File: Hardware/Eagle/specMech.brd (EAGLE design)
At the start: 142.2 x 121.9 mm, 80 parts, among them J1 PINHD-1X8-MOLEX-SHROUD, J2 JST-2-PIN-2B-PH-K-S(LF)(SN), J3 PINHD-1X8-MOLEX-SHROUD, J4 PINHD-1X8-MOLEX-SHROUD, J6 Molex 0022232081, J8 Molex 0022232081, U1 MCP23008-E/SO, U10 ADS1115, U11 MCP23008-E/SO, U12 74HC2G17TSSOP-6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

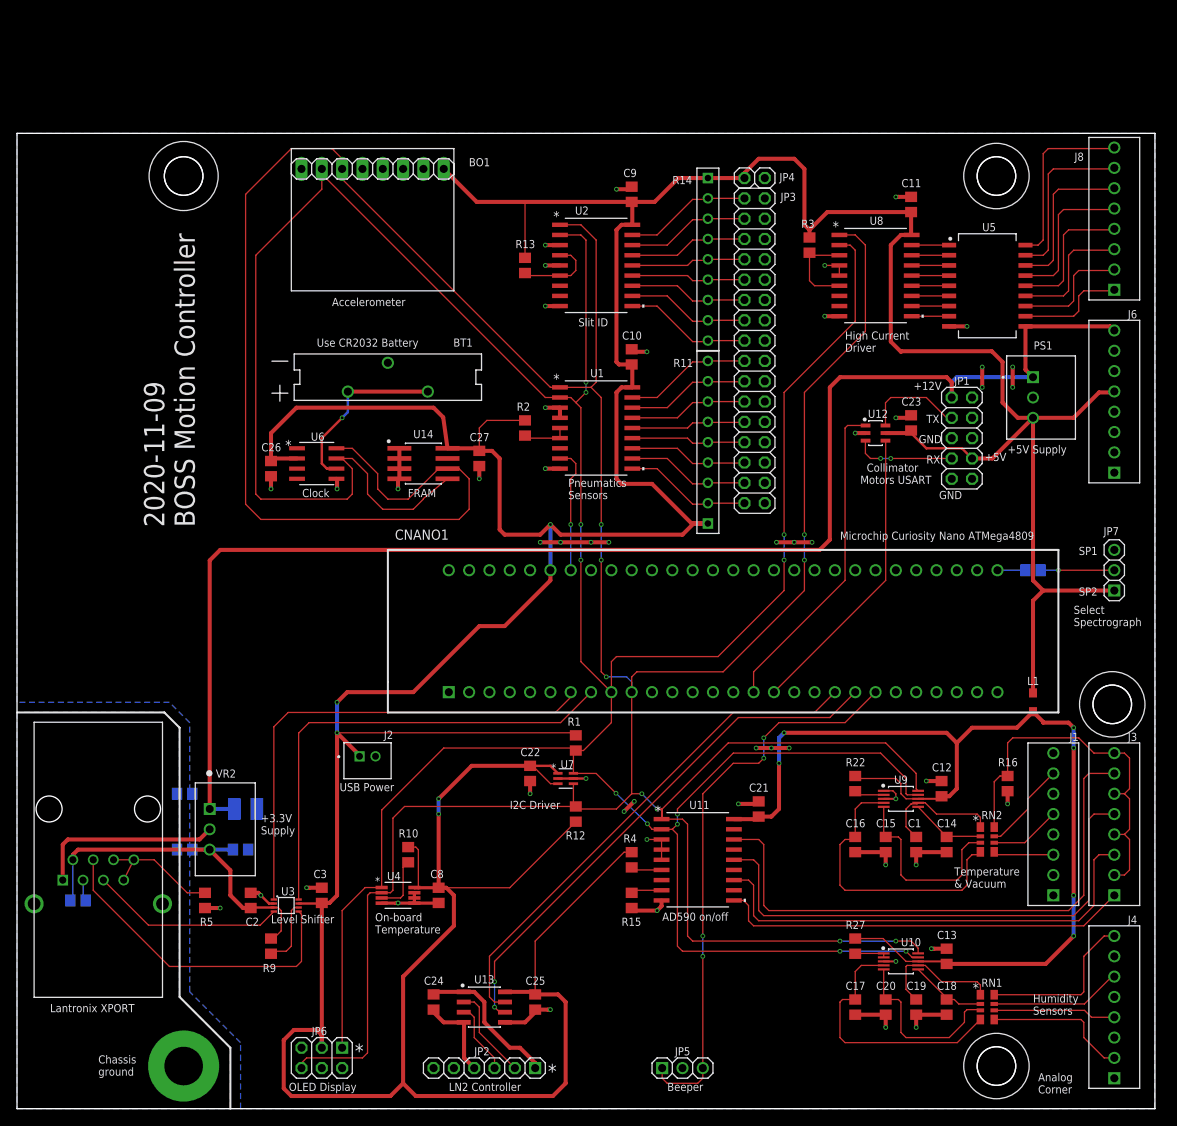
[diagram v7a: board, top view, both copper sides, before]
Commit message: Added test points, changed conflicting i2c address
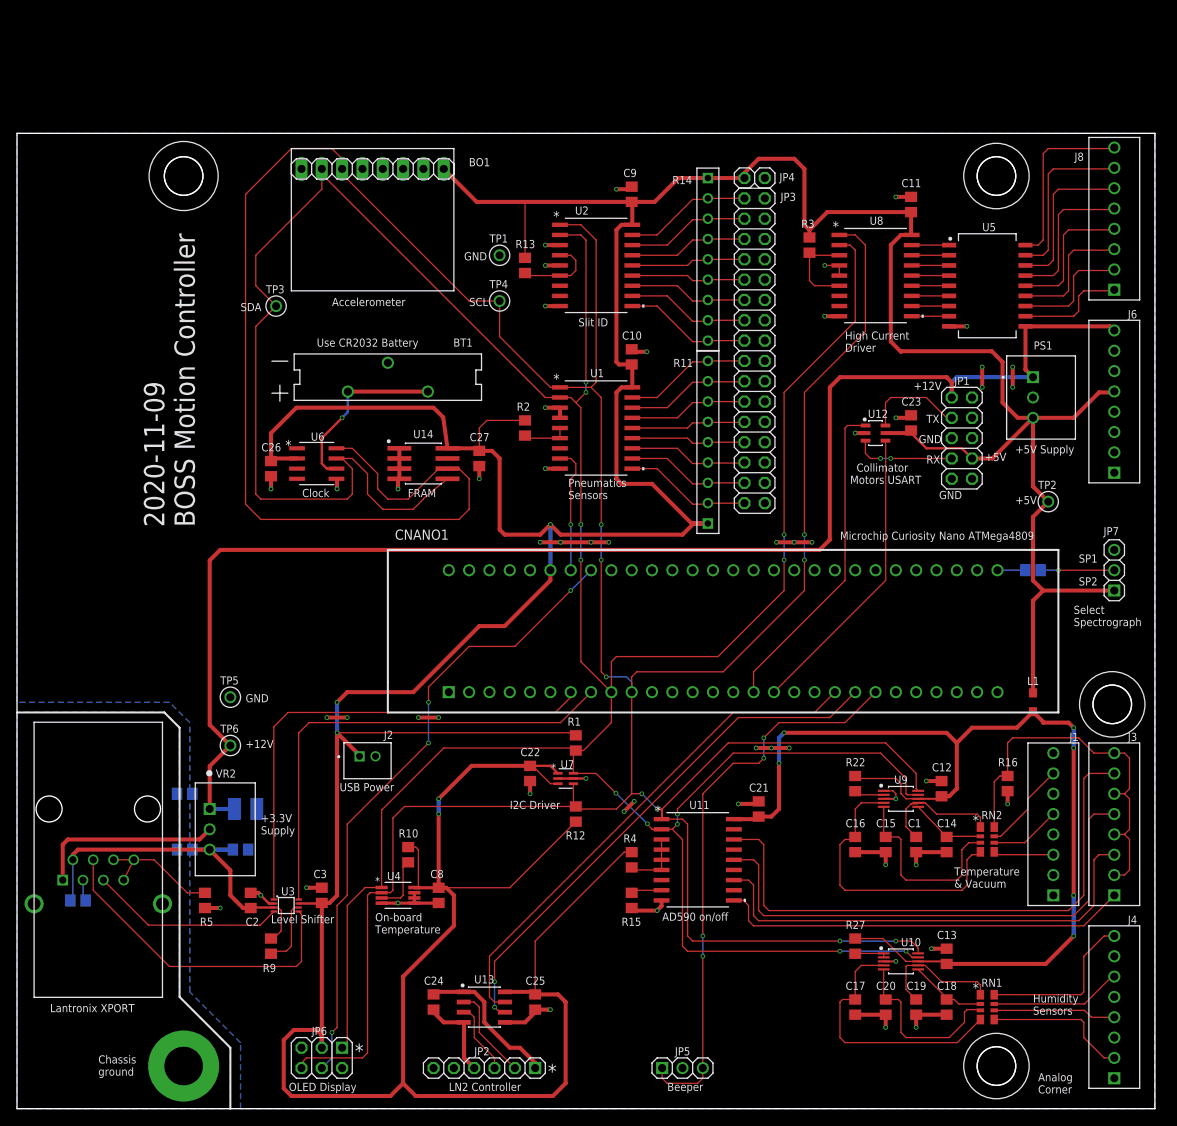
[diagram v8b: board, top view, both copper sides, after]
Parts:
- added TP1, TP5: TP5000-TESTPOINT-BLK, AUmlib:TP5000-TESTPOINT-BLK
- added TP2: TP5000-TESTPOINT-RED, AUmlib:TP5000-TESTPOINT-RED
- added TP3: TP5000-TESTPOINT-BLU, AUmlib:TP5000-TESTPOINT-BLU
- added TP4: TP5000-TESTPOINT-YEL, AUmlib:TP5000-TESTPOINT-YEL
- added TP6: TP5000-TESTPOINT-ORG, AUmlib:TP5000-TESTPOINT-ORG
- J7: value (none) -> Lantronix XPORT
- R10, R6: value (none) -> 10K
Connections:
- net +12V: now also TP6.P$1
- net +5V: now also TP2.P$1
- net GND: now also TP1.P$1, TP5.P$1; no longer U11.3, U11.4, U11.5
- net N$5: now also U11.3, U11.4, U11.5
- net OL/RST: now also CNANO1.PD6-AIN6
- net SCL: now also TP4.P$1
- net SDA: now also TP3.P$1
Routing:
- net OL/RST: track 0.00 -> 79.5 mm, vias 0 -> 4
- net N$5: track 3.87 -> 7.68 mm
- net SCL: track 479.7 -> 481.9 mm
- net +12V: track 180.1 -> 182.3 mm
- net SDA: track 438.4 -> 440.1 mm
- net +5V: track 644.9 -> 646.5 mm
- net GND: track 155.6 -> 156.4 mm, vias 52 -> 55
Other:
- board text added: "SCL"
- board text added: "SDA"
